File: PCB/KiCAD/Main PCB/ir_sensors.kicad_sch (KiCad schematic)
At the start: 13 parts, among them J1 Conn_02x03_Odd_Even, U2 ATmega328PB-A, Y1 Crystal

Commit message: More work to main PCB
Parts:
- added C32, C33: 100nF, Capacitor_SMD:C_0805_2012Metric_Pad1.18x1.45mm_HandSolder, symbol Device:C
- added C9: C_Polarized, Capacitor_SMD:CP_Elec_4x5.4, symbol Device:C_Polarized
- added IC1: TSSP4038, TSOP4038:TSSP4038, symbol TSSP4038:TSSP4038
- added IC2, IC3: ADG608BRZ, ADG608BRZ:SOIC127P600X175-16N, symbol ADG608BRZ:ADG608BRZ
- added R19: 100, Resistor_SMD:R_0805_2012Metric_Pad1.20x1.40mm_HandSolder, symbol Device:R
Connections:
- net +5V: now also C32.1, C33.1, IC2.13 (VDD), IC2.2 (EN), IC3.13 (VDD), IC3.2 (EN), R19.1
- net GND: now also C32.2, C33.2, C9.2, IC1.2 (GND), IC2.14 (GND), IC2.3 (VSS), IC3.14 (GND), IC3.3 (VSS)
- new net: C9.1, IC1.3 (VS), R19.2
- new net: IC1.1 (OUT), IC2.4 (S1)

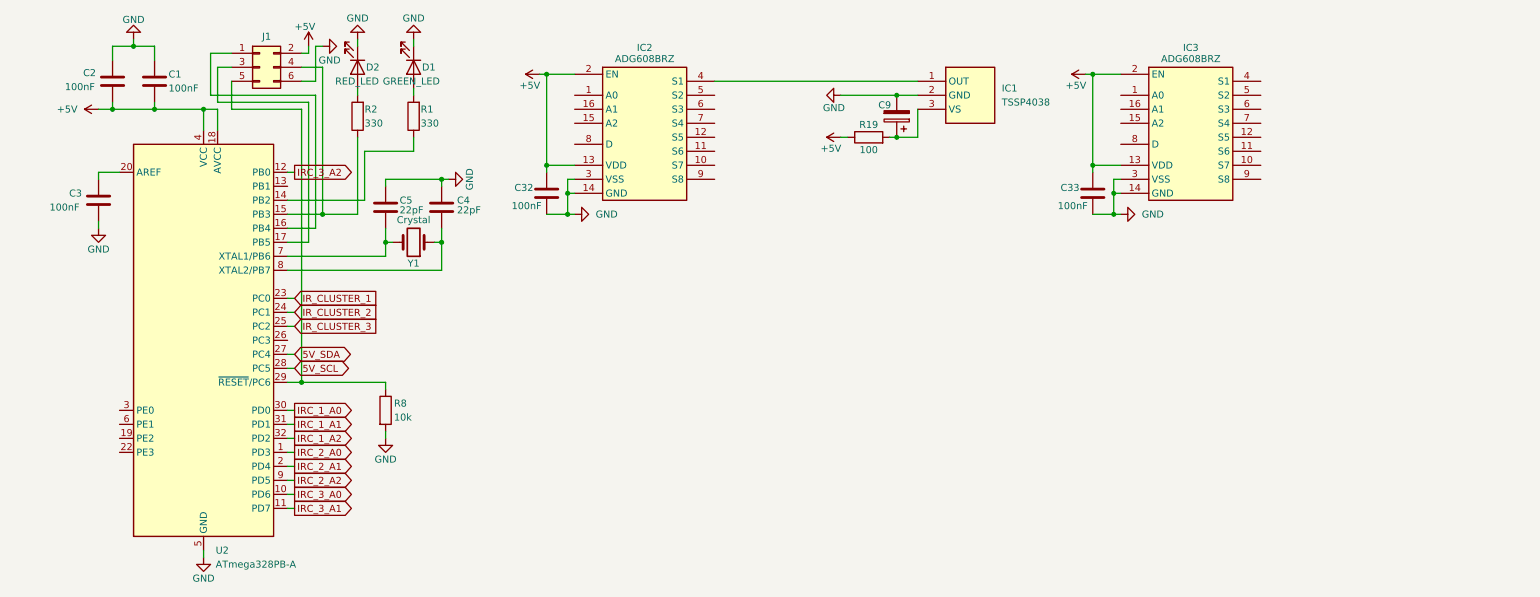
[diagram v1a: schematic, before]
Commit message: More work to the Main PCB and refinement of Via sizes
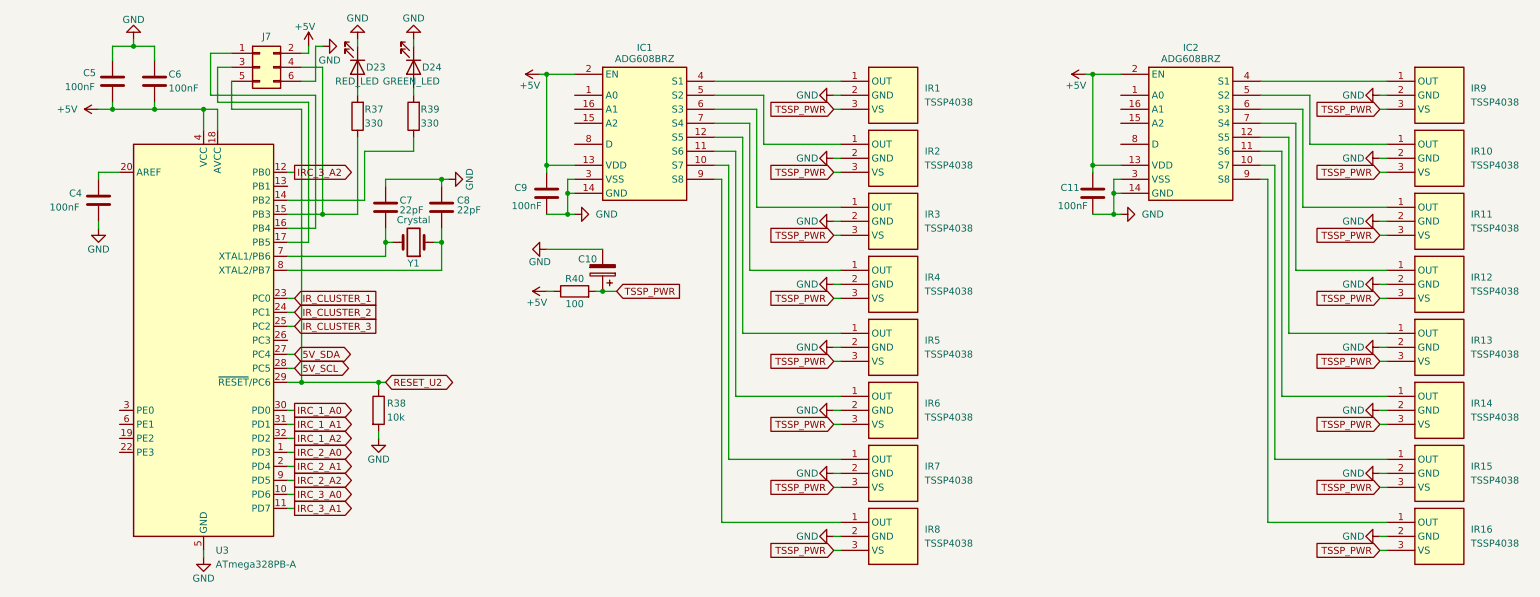
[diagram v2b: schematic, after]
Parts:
- added IR10, IR11, IR12, IR13, IR14, IR15, IR16, IR2, IR3, IR4, IR5, IR6, IR7, IR8, IR9: TSSP4038, TSOP4038:TSSP4038, symbol TSSP4038:TSSP4038
- C10: renamed from C9; value C_Polarized -> 4.7uF
- renumbered C33 to C11, C3 to C4, C2 to C5, C1 to C6, C5 to C7, C4 to C8, C32 to C9, D2 to D23, D1 to D24, IC2 to IC1, IC3 to IC2, IC1 to IR1, J1 to J7, R2 to R37, R8 to R38, R1 to R39, R19 to R40, U2 to U3
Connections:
- net GND: now also IR10.2 (GND), IR11.2 (GND), IR12.2 (GND), IR13.2 (GND), IR14.2 (GND), IR15.2 (GND), IR16.2 (GND), IR2.2 (GND), IR3.2 (GND), IR4.2 (GND), IR5.2 (GND), IR6.2 (GND), IR7.2 (GND), IR8.2 (GND), IR9.2 (GND)
- net TSSP_PWR: now reaches C10.1, IR1.3 (VS), R40.2
- net TSSP_PWR: now also IR10.3 (VS), IR11.3 (VS), IR12.3 (VS), IR13.3 (VS), IR14.3 (VS), IR15.3 (VS), IR16.3 (VS), IR2.3 (VS), IR3.3 (VS), IR4.3 (VS), IR5.3 (VS), IR6.3 (VS), IR7.3 (VS), IR8.3 (VS), IR9.3 (VS)
- net RESET_U2: now reaches J7.5 (Pin_5), R38.1, U3.29 (~{RESET}/PC6)
- net at IC2.10 (S7): now also IR15.1 (OUT)
- net at IC2.11 (S6): now also IR14.1 (OUT)
- net at IC2.12 (S5): now also IR13.1 (OUT)
- net at IC2.4 (S1): now also IR9.1 (OUT)
- net at IC2.5 (S2): now also IR10.1 (OUT)
- net at IC2.6 (S3): now also IR11.1 (OUT)
- net at IC2.7 (S4): now also IR12.1 (OUT)
- net at IC2.9 (S8): now also IR16.1 (OUT)
- net at IC1.10 (S7): now also IR7.1 (OUT)
- net at IC1.11 (S6): now also IR6.1 (OUT)
- net at IC1.12 (S5): now also IR5.1 (OUT)
- net at IC1.5 (S2): now also IR2.1 (OUT)
- net at IC1.6 (S3): now also IR3.1 (OUT)
- net at IC1.7 (S4): now also IR4.1 (OUT)
- net at IC1.9 (S8): now also IR8.1 (OUT)
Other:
- moved on the sheet: C10, IR1, R38, R40

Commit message: Changes to the main PCB
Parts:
- removed C4, C5, C6: 100nF, Capacitor_SMD:C_0805_2012Metric_Pad1.18x1.45mm_HandSolder, symbol Device:C
- removed C7, C8: 22pF, Capacitor_SMD:C_0805_2012Metric_Pad1.18x1.45mm_HandSolder, symbol Device:C
- removed D23: RED_LED, LED_SMD:LED_0805_2012Metric_Pad1.15x1.40mm_HandSolder, symbol Device:LED
- removed D24: GREEN_LED, LED_SMD:LED_0805_2012Metric_Pad1.15x1.40mm_HandSolder, symbol Device:LED
- removed J7: Conn_02x03_Odd_Even, Connector_IDC:IDC-Header_2x03_P2.54mm_Vertical_SMD, symbol Connector_Generic:Conn_02x03_Odd_Even
- removed R37, R39: 330, Resistor_SMD:R_0805_2012Metric_Pad1.20x1.40mm_HandSolder, symbol Device:R
- removed R38: 10k, Resistor_SMD:R_0805_2012Metric_Pad1.20x1.40mm_HandSolder, symbol Device:R
- removed U3: ATmega328PB-A, Package_QFP:TQFP-32_7x7mm_P0.8mm, symbol MCU_Microchip_ATmega:ATmega328PB-A
- removed Y1: Crystal, Crystal:Crystal_SMD_HC49-SD, symbol Device:Crystal
- renumbered C9 to C1, C10 to C2, C11 to C3, R40 to R15
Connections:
- net TSSP_2_A0: now reaches IC2.1 (A0)
- net TSSP_2_A2: now reaches IC2.15 (A2)
- net TSSP_2_A1: now reaches IC2.16 (A1)
- net TSSP_2_OUT: now reaches IC2.8 (D)
- net TSSP_1_A0: now reaches IC1.1 (A0)
- net TSSP_1_A2: now reaches IC1.15 (A2)
- net TSSP_1_A1: now reaches IC1.16 (A1)
- net TSSP_1_OUT: now reaches IC1.8 (D)
- net +5V renamed +3V3_4_0
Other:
- moved on the sheet: C1, C2, C3, IC1, IC2, IR1, IR10, IR11, IR12, IR13, IR14, IR15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

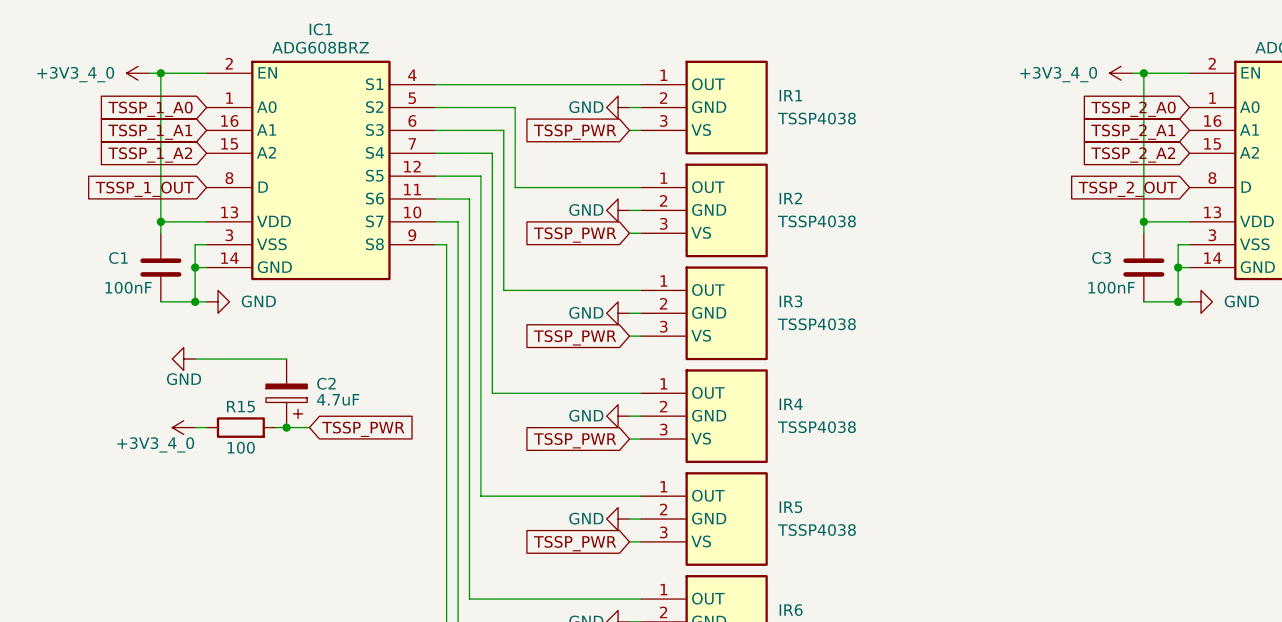
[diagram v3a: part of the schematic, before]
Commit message: New motor controllers for the main PCB
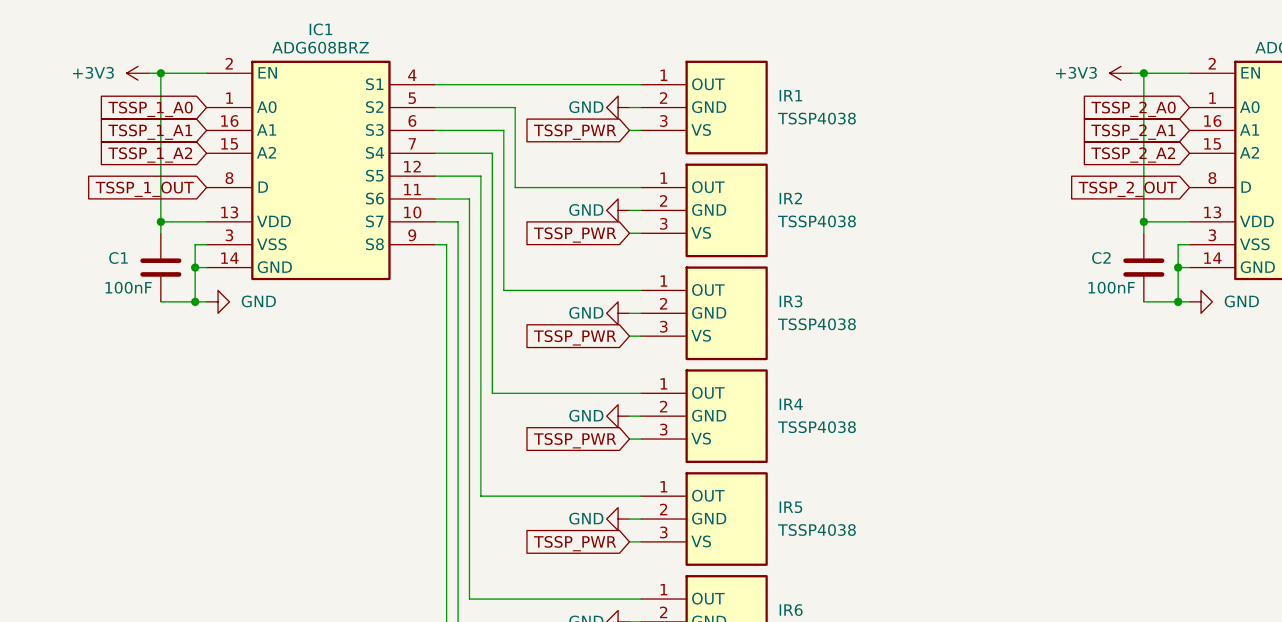
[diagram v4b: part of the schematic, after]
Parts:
- removed C2: 4.7uF, Capacitor_SMD:CP_Elec_4x5.4, symbol Device:C_Polarized
- removed R15: 100, Resistor_SMD:R_0805_2012Metric_Pad1.20x1.40mm_HandSolder, symbol Device:R
- renumbered C3 to C2
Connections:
- net +3V3_4_0 renamed +3V3

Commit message: Redone main PCB traces and started lower PCB
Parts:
- IR1, IR10, IR11, IR12, IR13, IR14, IR15, IR16, IR2, IR3, IR4, IR5, IR6, IR7, IR8, IR9: value TSSP4038 -> TSOP34840
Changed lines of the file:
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@@
 			)
 		)
-		(property "Value" "TSSP4038"
+		(property "Value" "TSOP34840"
 			(at 199.39 38.0999 0)
 			(effects
@@
 			)
 		)
-		(property "Value" "TSSP4038"
+		(property "Value" "TSOP34840"
 			(at 90.17 38.0999 0)
 			(effects
@@
 			)
 		)
-		(property "Value" "TSSP4038"
+		(property "Value" "TSOP34840"
 			(at 199.39 72.3899 0)
 			(effects
@@
 			)
 		)
-		(property "Value" "TSSP4038"
+		(property "Value" "TSOP34840"
 			(at 199.39 95.2499 0)
 			(effects
@@
 			)
 		)
-		(property "Value" "TSSP4038"
+		(property "Value" "TSOP34840"
 			(at 90.17 60.9599 0)
 			(effects
@@
 			)
 		)
-		(property "Value" "TSSP4038"
+		(property "Value" "TSOP34840"
 			(at 90.17 106.6799 0)
 			(effects
@@
 			)
 		)
-		(property "Value" "TSSP4038"
+		(property "Value" "TSOP34840"
 			(at 90.17 49.5299 0)
 			(effects
@@
 			)
 		)
-		(property "Value" "TSSP4038"
+		(property "Value" "TSOP34840"
 			(at 90.17 95.2499 0)
 			(effects
@@
 			)
 		)
-		(property "Value" "TSSP4038"
+		(property "Value" "TSOP34840"
 			(at 90.17 72.3899 0)
 			(effects
@@
 			)
 		)
-		(property "Value" "TSSP4038"
+		(property "Value" "TSOP34840"
 			(at 199.39 60.9599 0)
 			(effects
@@
 			)
 		)
-		(property "Value" "TSSP4038"
+		(property "Value" "TSOP34840"
 			(at 199.39 83.8199 0)
 			(effects
@@
 			)
 		)
-		(property "Value" "TSSP4038"
+		(property "Value" "TSOP34840"
 			(at 90.17 26.6699 0)
 			(effects
@@
 			)
 		)
-		(property "Value" "TSSP4038"
+		(property "Value" "TSOP34840"
 			(at 90.17 83.8199 0)
 			(effects
@@
 			)
 		)
-		(property "Value" "TSSP4038"
+		(property "Value" "TSOP34840"
 			(at 199.39 106.6799 0)
 			(effects
@@
 			)
 		)
-		(property "Value" "TSSP4038"
+		(property "Value" "TSOP34840"
 			(at 199.39 26.6699 0)
 			(effects
@@
 			)
 		)
-		(property "Value" "TSSP4038"
+		(property "Value" "TSOP34840"
 			(at 199.39 49.5299 0)
 			(effects
